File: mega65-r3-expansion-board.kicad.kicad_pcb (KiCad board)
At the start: 4 copper layers, 215 x 126.9 mm, 97 parts, among them J1 Conn_01x04, J10 PMOD2, J11 Conn_02x05_Odd_Even, J12 Conn_02x17_Odd_Even, J13 Conn_02x17_Odd_Even, J14 Component A/V, J15 ESP32 Connector, J2 Conn_01x04, J3 C64_User_Port, J4 Mini-DIN-8-With-Shield, J5 C64_Tape_Port, J6 OKR-T/3-W12-C, J7 Conn_02x06_Odd_Even, J8 Conn_02x06_Odd_Even, J9 PMOD1, U1 74HC595, U10 74LS125, U11 74HC595, U12 74LS125, U2 74LVC165, U3 74LS125, U4 74HC595, U5 74LVC165, U6 74HC595, U7 74LVC165, U8 74LS125, U9 74LS125

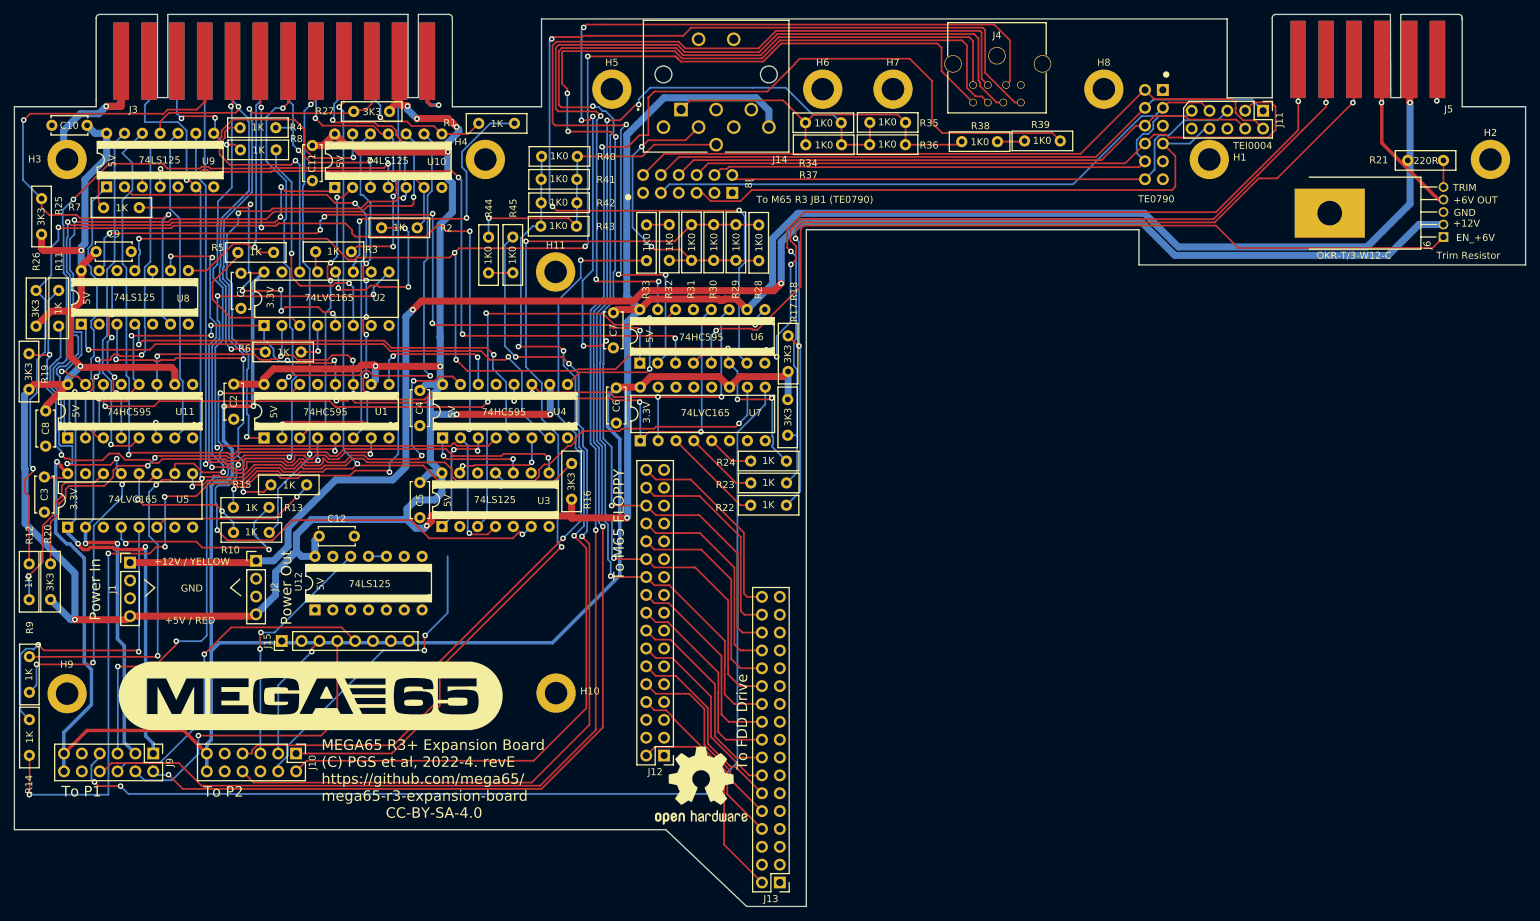
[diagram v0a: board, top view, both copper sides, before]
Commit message: fix design rule check errors and false alarms
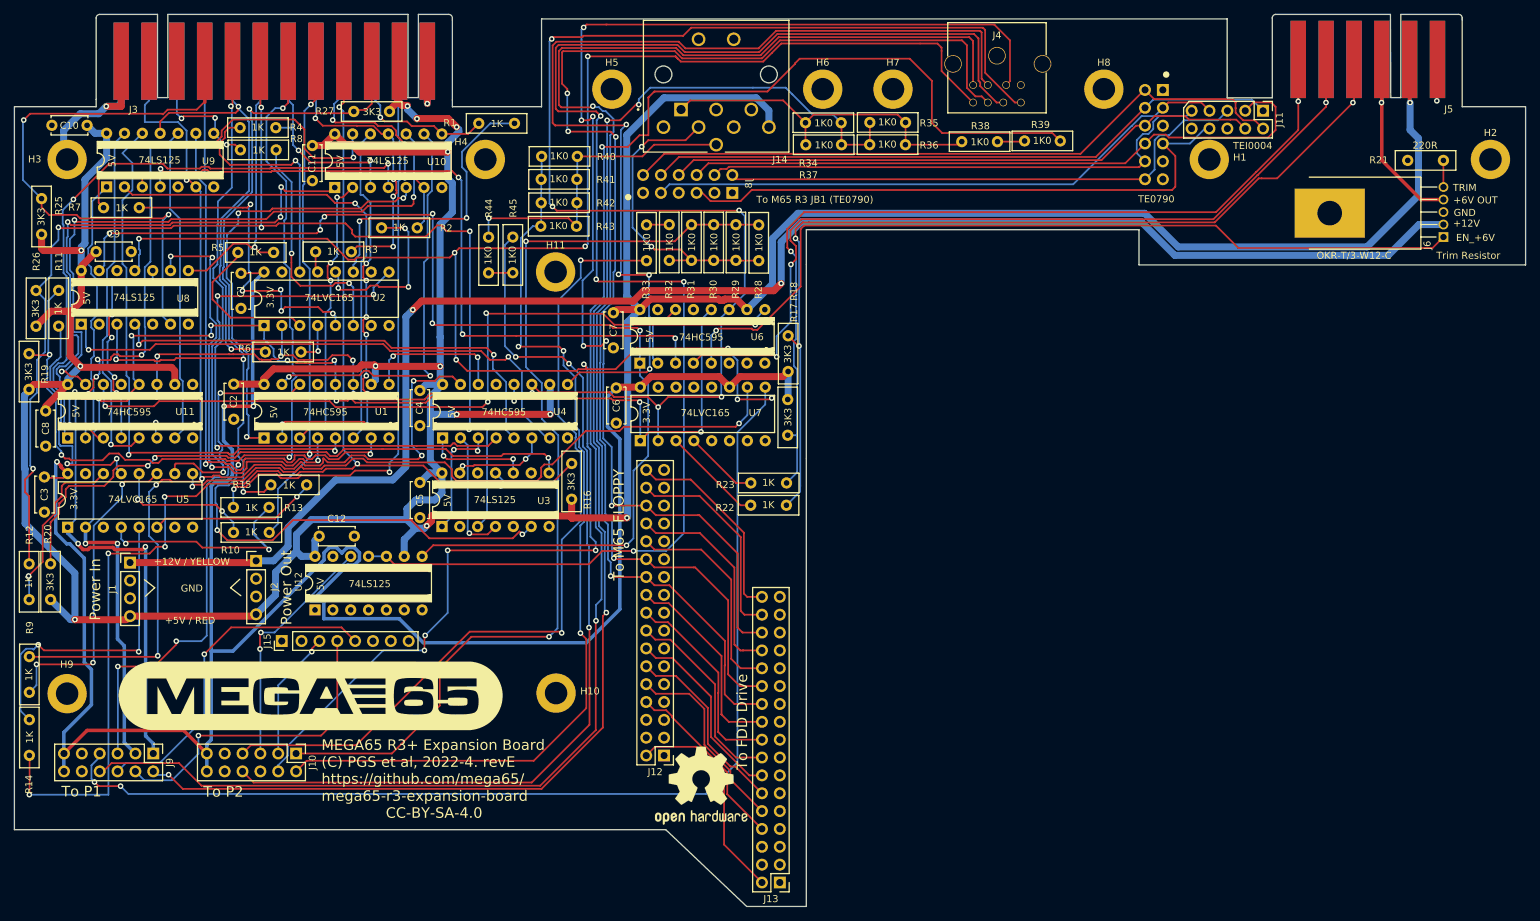
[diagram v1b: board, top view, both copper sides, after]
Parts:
- removed R24: 1K, snapeda:Labeled Resistor
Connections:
- U6 pad 15: 1565_LD -> unconnected-(U6-QA-Pad15)
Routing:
- net 1565_LD: track 127.8 -> 207.8 mm, vias 3 -> 4
- net EN_1565_SERIO: track 104.1 -> 161.5 mm, vias 6 -> 7
- net 1565_SERIO: track 282.6 -> 322.7 mm, vias 10 -> 13
- net +3V3: track 279.6 -> 310.6 mm
- net GND: track 55.4 -> 40.7 mm
- net EXP_CLOCK: track 334.1 -> 326.3 mm
- net Net-(U7-D6): track 6.75 -> 0.00 mm
- net COMP_LUMA5: track 132.9 -> 138.9 mm
- net COMP_LUMA2: track 114.3 -> 118.9 mm
- net 1565_RST: track 133.9 -> 131.6 mm
- net /User Port, Tape Port & C1565 Port/TAPE_MOTOR: track 30.4 -> 32.1 mm
- net /User Port, Tape Port & C1565 Port/CNT1_O: track 14.7 -> 13.9 mm
- net COMP_CHROMA5: track 134.2 -> 133.5 mm
- net Net-(U4-QH'): track 24.1 -> 24.8 mm
- net COMP_COMP2: track 241.3 -> 242.0 mm
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
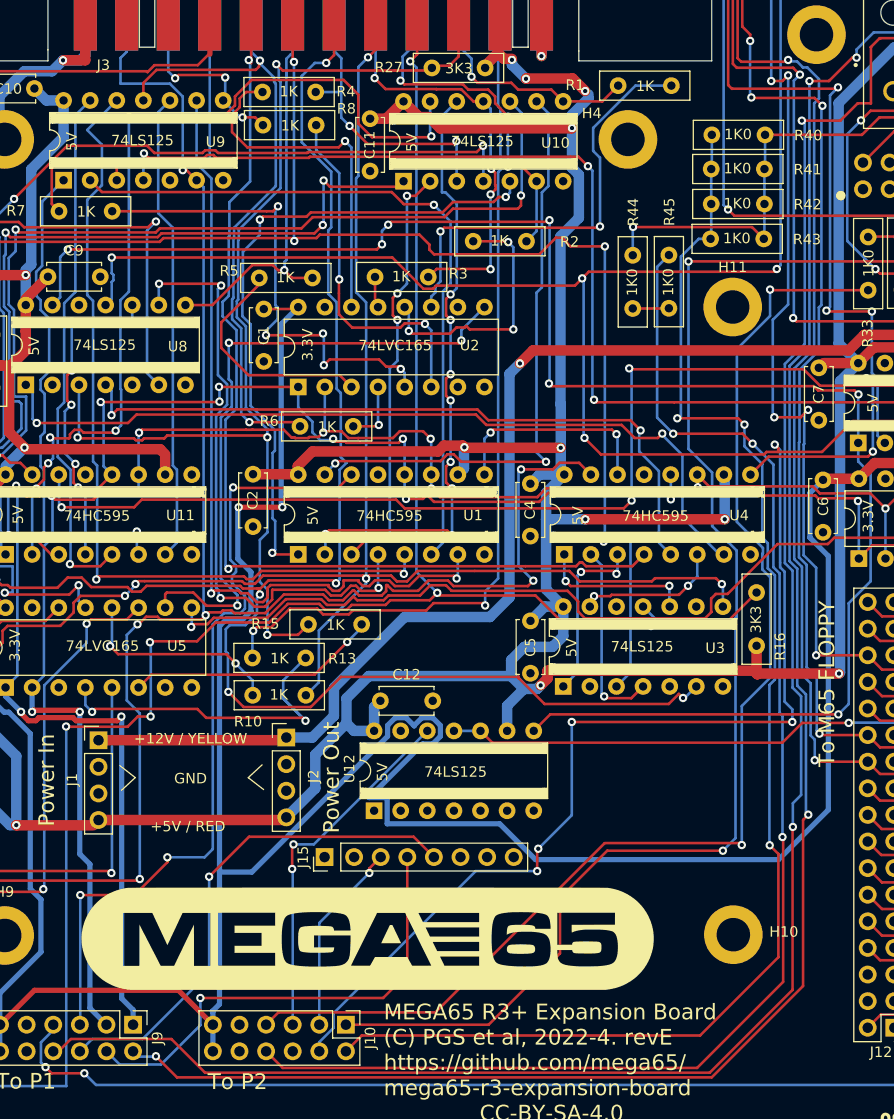
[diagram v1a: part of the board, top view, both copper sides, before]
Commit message: fix and finish routing 3.3V SERIO and related things
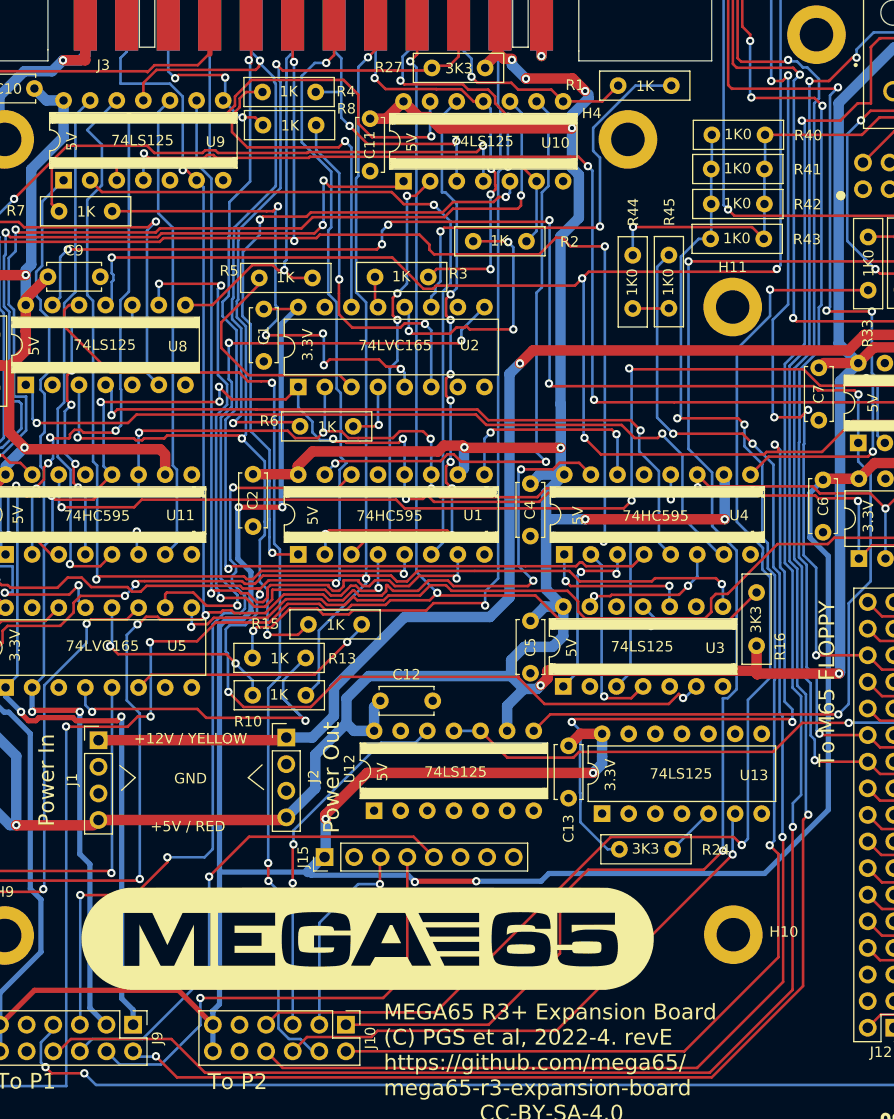
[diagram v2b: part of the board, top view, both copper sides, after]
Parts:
- added C13: 0.1uF, Capacitor_THT:C_Disc_D5.0mm_W2.5mm_P5.00mm, F.Cu at (80.2, 105.6)
- added R24: 3K3, snapeda:Labeled Resistor, F.Cu at (85.0, 115.5)
- added U13: 74LS125, snapeda:DIP-14_74LS06, F.Cu at (83.4, 112.1)
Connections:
- net C1565_LD_3V3 renamed 1565_LD_3V3
- J10 pad 4: 1565_SERIO -> 1565_SERIO_O
- J10 pad 6: AUX4 -> 1565_SERIO_I
- J15 pad 1: +3.3V -> +3V3
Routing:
- net 1565_SERIO_O: track 0.00 -> 92.7 mm, vias 0 -> 3
- net 1565_SERIO_I: track 0.00 -> 53.8 mm, vias 0 -> 1
- net 1565_SERIO: track 322.7 -> 292.8 mm, vias 13 -> 11
- net +3V3: track 310.6 -> 324.5 mm, vias 3 -> 7
- net Net-(R24-Pad2): track 0.00 -> 4.84 mm
- net /User Port, Tape Port & C1565 Port/RESET_N: track 110.4 -> 108.1 mm
- net /User Port, Tape Port & C1565 Port/DATA_5: track 63.4 -> 65.1 mm
- net WIFI_EN: track 18.4 -> 19.7 mm
- net 1565_LD: track 207.8 -> 208.9 mm
- net EXP_LATCH: track 201.8 -> 202.8 mm
- net 1565_LD_3V3: track 34.6 -> 35.3 mm

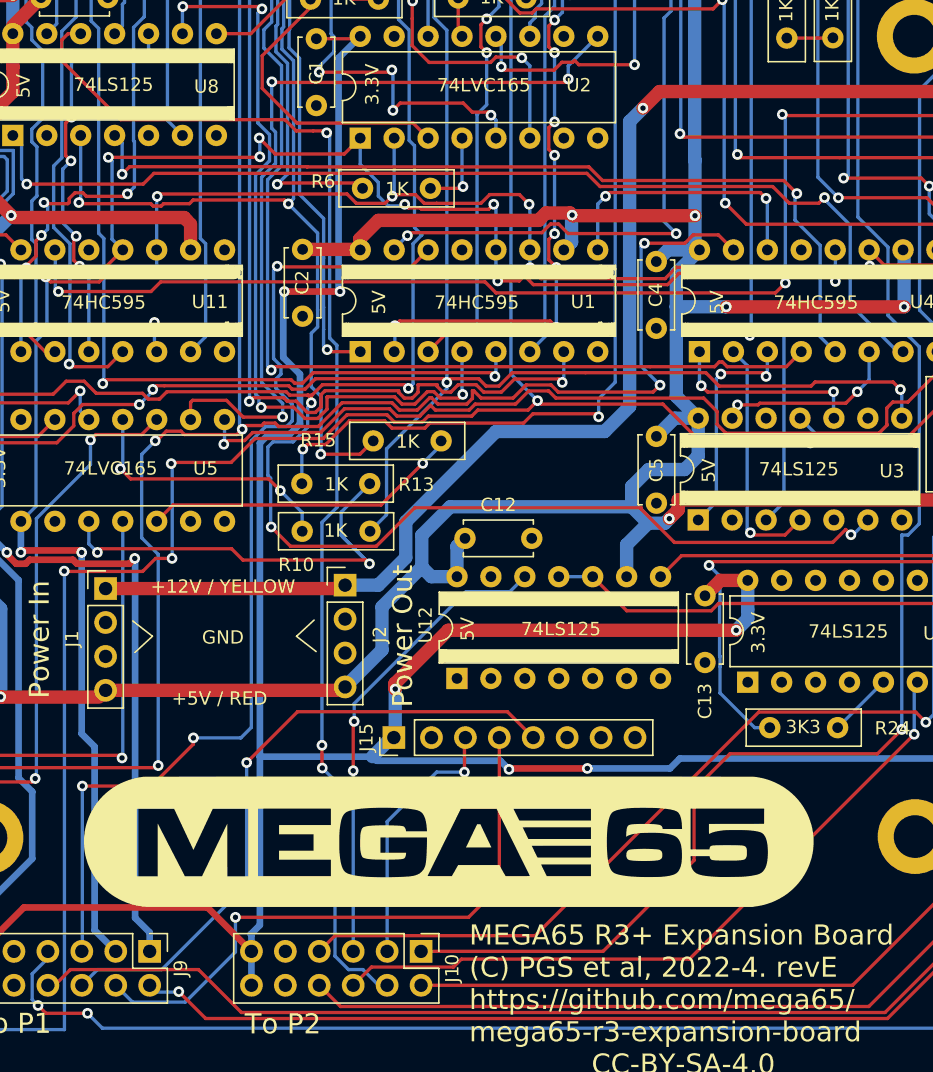
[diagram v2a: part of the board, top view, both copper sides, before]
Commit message: fatten 3.3V rail part of its length
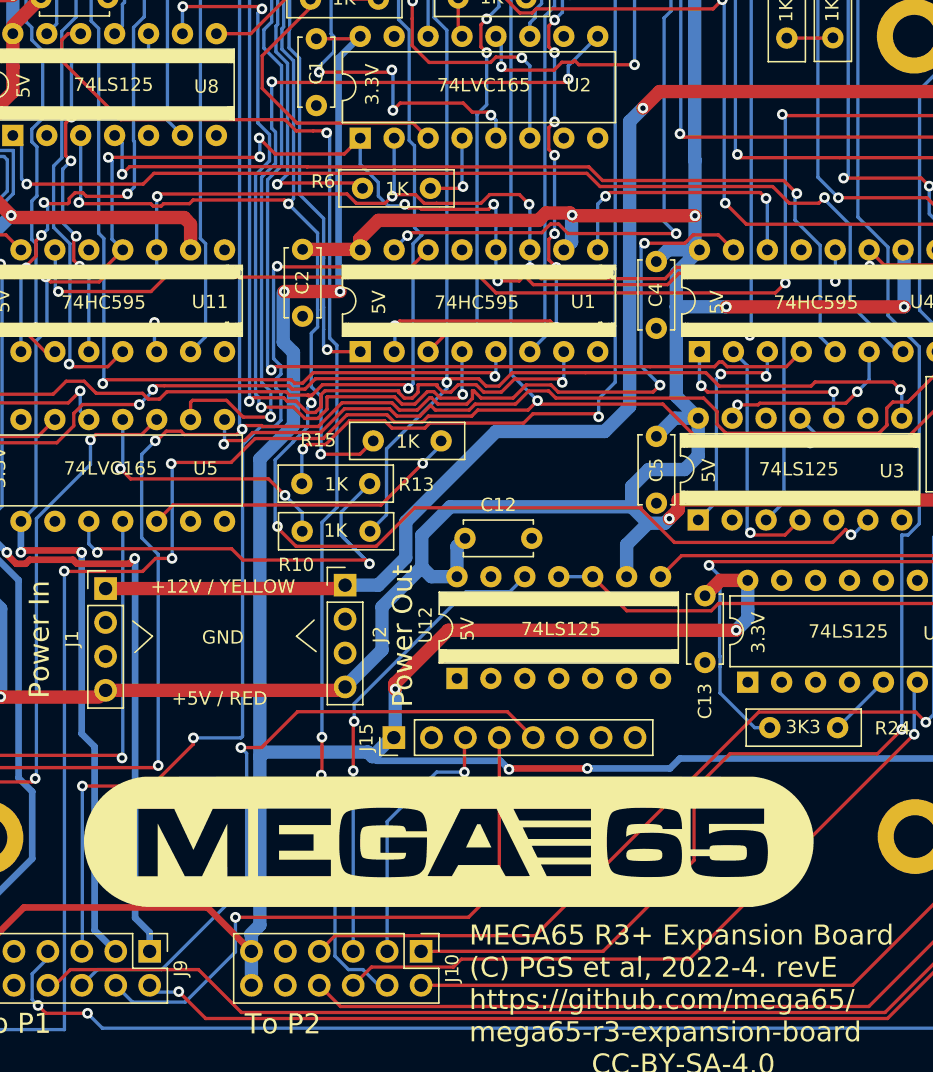
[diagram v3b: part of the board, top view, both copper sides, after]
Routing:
- net /User Port, Tape Port & C1565 Port/CNT2: track 184.1 -> 182.6 mm
- net UART_TX: track 48.4 -> 49.7 mm
- net Net-(U2-Q7): track 61.5 -> 60.2 mm
- net +3V3: track 324.5 -> 323.4 mm
- net EXP_WDATA: track 76.2 -> 75.2 mm
